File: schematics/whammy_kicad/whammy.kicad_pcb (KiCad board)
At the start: 2 copper layers, 54 parts, among them Q1 2SK2013, Q2 2SJ313, Q3 2SK2013, Q4 2SJ313, U1 OPA2604, U4 4N35, U5 4N35

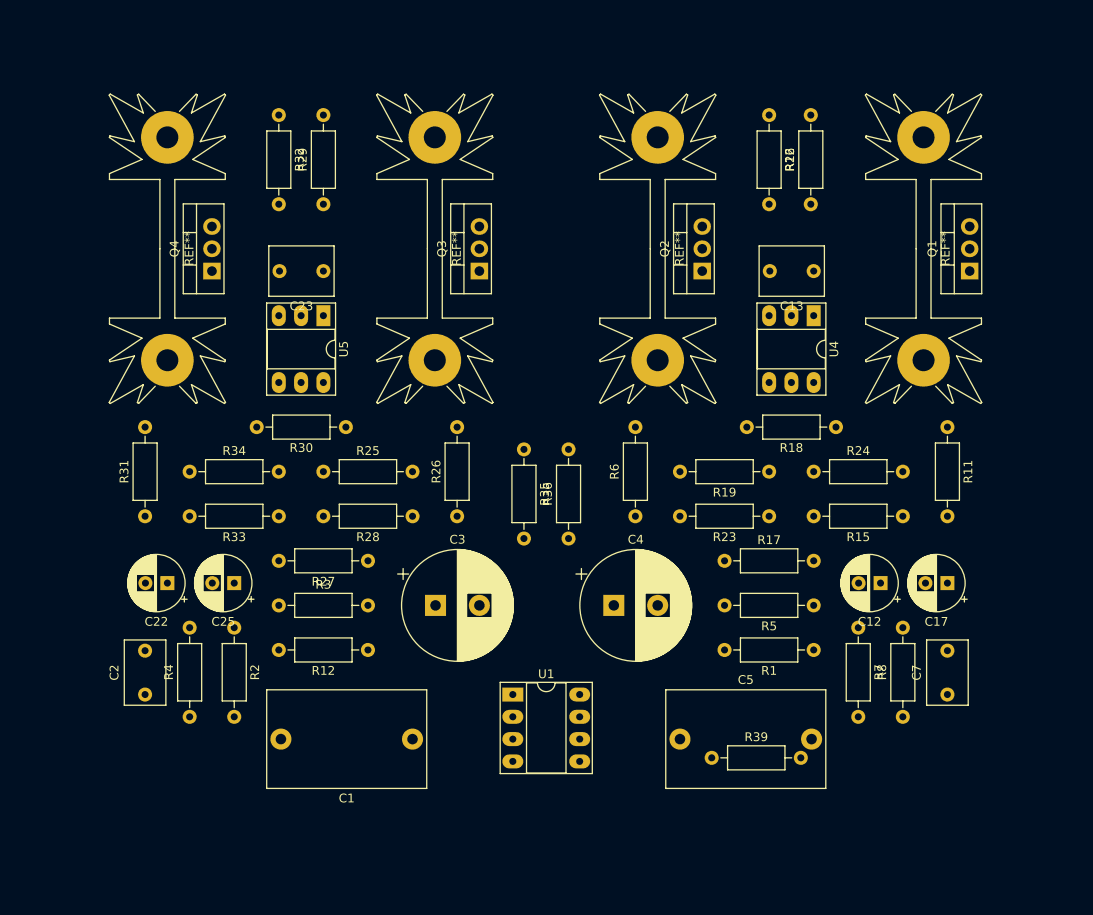
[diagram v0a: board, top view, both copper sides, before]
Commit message: First PCB version with single heatsinks.
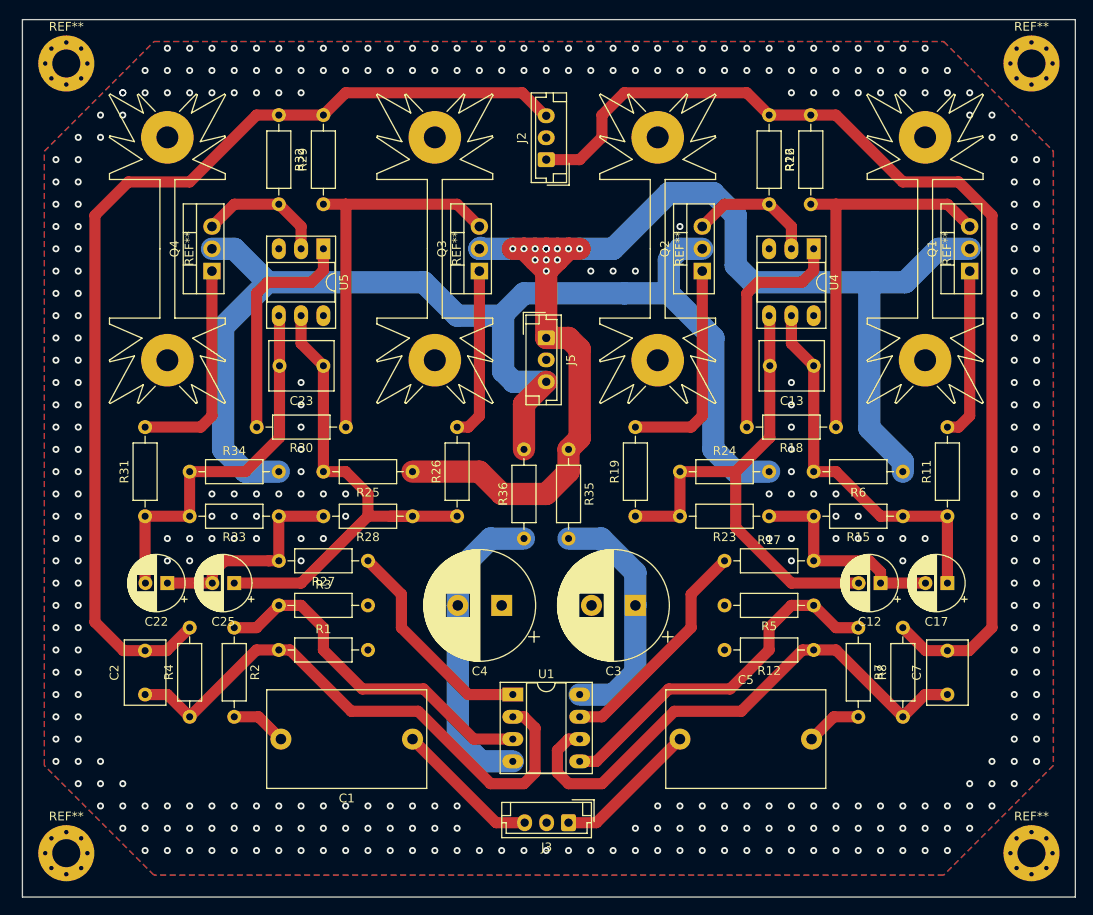
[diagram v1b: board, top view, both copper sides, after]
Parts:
- removed R39: 2K2, Resistor_THT:R_Axial_DIN0207_L6.3mm_D2.5mm_P10.16mm_Horizontal
- added J2: Conn_01x03, Connector_JST:JST_EH_B3B-EH-A_1x03_P2.50mm_Vertical, F.Cu at (139.7, 61.0)
- added J3: Conn_01x03, Connector_JST:JST_EH_B3B-EH-A_1x03_P2.50mm_Vertical, F.Cu at (142.2, 136.5)
- added J5: Conn_01x03, Connector_JST:JST_EH_B3B-EH-A_1x03_P2.50mm_Vertical, F.Cu at (139.7, 81.3)
- added REF**: MountingHole_3.2mm_M3_Pad_Via, MountingHole:MountingHole_3.2mm_M3_Pad_Via, F.Cu at (195.0, 140.0)
- added REF**: MountingHole_3.2mm_M3_Pad_Via, MountingHole:MountingHole_3.2mm_M3_Pad_Via, F.Cu at (85.0, 140.0)
- added REF**: MountingHole_3.2mm_M3_Pad_Via, MountingHole:MountingHole_3.2mm_M3_Pad_Via, F.Cu at (195.0, 50.0)
- added REF**: MountingHole_3.2mm_M3_Pad_Via, MountingHole:MountingHole_3.2mm_M3_Pad_Via, F.Cu at (85.0, 50.0)
- moved R1 61.0 mm to (109.2, 116.8), turned to 0 degrees
- moved R12 50.8 mm to (170.2, 116.8)
- moved R6 30.9 mm to (180.3, 96.5), turned to 180 degrees
- moved C3 22.8 mm to (149.9, 111.8), turned to 180 degrees
- moved R19 16.1 mm to (149.9, 101.6), turned to 90 degrees
- moved R24 15.2 mm to (154.9, 96.5)
- moved C4 12.8 mm to (134.6, 111.8), turned to 180 degrees
- moved C13 10.8 mm to (170.2, 84.5)
- moved C23 10.8 mm to (114.3, 84.5)
- moved R11 10.2 mm to (185.4, 101.6), turned to 90 degrees
- moved R25 10.2 mm to (124.5, 96.5), turned to 180 degrees
- moved U4 7.62 mm to (170.2, 71.1)
- moved U5 7.62 mm to (114.3, 71.1)
- moved R35 5.08 mm to (142.2, 94.0)
- moved R36 5.08 mm to (137.2, 104.1)
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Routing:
- net +15V: track 0.00 -> 154.9 mm, vias 0 -> 13
- net -15V: track 0.00 -> 140.8 mm
- net LEFT_OUT: track 0.00 -> 120.6 mm
- net RIGHT_OUT: track 0.00 -> 117.9 mm
- net Net-(C2-Pad1): track 0.00 -> 63.6 mm
- net Net-(C7-Pad1): track 0.00 -> 61.1 mm
- net Net-(C12-Pad2): track 0.00 -> 58.9 mm
- net Net-(C23-Pad1): track 0.00 -> 58.6 mm
- net Net-(Q1-Pad3): track 0.00 -> 44.6 mm
- net Net-(Q3-Pad3): track 0.00 -> 44.2 mm
- net Net-(C13-Pad1): track 0.00 -> 43.8 mm
- net Net-(C22-Pad2): track 0.00 -> 43.6 mm
- net Net-(R5-Pad1): track 0.00 -> 41.7 mm
- net Net-(R2-Pad1): track 0.00 -> 40.6 mm
- net Net-(C4-Pad2): track 0.00 -> 35.5 mm
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- added copper zone on B.Cu, net GND
- added copper zone on F.Cu, net GND
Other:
- board outline added: 120 x 100 mm

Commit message: Final version
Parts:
- removed the REF** at (195.0, 140.0)
- removed the REF** at (195.0, 50.0)
- added ?: MountingHole_3.2mm_M3_Pad_Via, MountingHole:MountingHole_3.2mm_M3_Pad_Via, F.Cu at (175.0, 135.0)
- added ?: MountingHole_3.2mm_M3_Pad_Via, MountingHole:MountingHole_3.2mm_M3_Pad_Via, F.Cu at (175.0, 50.0)
- added C26: 22uF/25V, Capacitor_THT:CP_Radial_D6.3mm_P2.50mm, F.Cu at (146.1, 119.4)
- added C27: 22uF/25V, Capacitor_THT:CP_Radial_D6.3mm_P2.50mm, F.Cu at (115.6, 119.4)
- C3, C4: value 220uF/50V -> 220uF/25V
- moved R7 25.3 mm to (151.1, 121.9), turned to 0 degrees
- moved R11 23.3 mm to (163.8, 92.7), turned to 0 degrees
- moved R6 19.1 mm to (161.3, 97.8), turned to 0 degrees
- moved R26 18.8 mm to (113.0, 92.7), turned to 0 degrees
- moved R35 16.6 mm to (133.3, 80.0)
- moved R36 16.6 mm to (128.3, 90.2)
- moved J5 15.5 mm to (130.8, 68.6)
- moved J2 15.3 mm to (128.3, 50.8), turned to 0 degrees
- moved J3 15.1 mm to (128.3, 130.8), turned to 0 degrees
- moved C7 14.0 mm to (171.4, 120.7)
- moved Q1 14.0 mm to (174.0, 74.9)
- moved R17 14.0 mm to (146.1, 108.0)
- moved R5 14.0 mm to (156.2, 113.0)
- moved R8 14.0 mm to (166.4, 125.7)
- moved REF** 14.0 mm to (168.9, 72.4)
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- renumbered REF** to ?
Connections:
- J2 pad 1: LEFT_OUT -> RIGHT_OUT
- J2 pad 3: RIGHT_OUT -> LEFT_OUT
- J3 pad 1: Net-(C5-Pad1) -> Net-(C1-Pad1)
- J3 pad 3: Net-(C1-Pad1) -> Net-(C5-Pad1)
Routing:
- net -15V: track 140.8 -> 113.8 mm
- net +15V: track 154.9 -> 138.7 mm, vias 13 -> 0
- net LEFT_OUT: track 120.6 -> 104.9 mm
- net Net-(R5-Pad1): track 41.7 -> 27.5 mm
- net RIGHT_OUT: track 117.9 -> 104.8 mm
- net Net-(R2-Pad1): track 40.6 -> 28.6 mm
- net Net-(R17-Pad1): track 26.1 -> 15.1 mm
- net Net-(R27-Pad1): track 25.1 -> 14.1 mm
- net Net-(C2-Pad1): track 63.6 -> 56.8 mm
- net Net-(C7-Pad1): track 61.1 -> 54.3 mm
- net Net-(C27-Pad1): track 0.00 -> 5.61 mm
- net Net-(C26-Pad1): track 0.00 -> 5.61 mm
- net Net-(C4-Pad2): track 35.5 -> 39.7 mm
- net Net-(C1-Pad1): track 16.7 -> 12.7 mm
- net Net-(C5-Pad1): track 16.6 -> 12.8 mm
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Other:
- board size 120 x 100 mm -> 100 x 95 mm
- net class Power added: clearance 0.5, trace_width 0.25, via_dia 0.8, via_drill 0.4
- board text added: "+VCC"
- board text added: "-VCC"
- board text added: "GND"
- board text added: "INPUT"
- board text added: "L-G-R"
- board text added: "OUTPUT"
- board text added: "POWER"
- board text added: "WHAMMY"
- board text added: "WHAMMY Headphone Amplifier"
